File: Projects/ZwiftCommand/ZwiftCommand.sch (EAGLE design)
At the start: 17 parts, among them M1 DMP2165UW, U1 BAT-HLD-001-THM

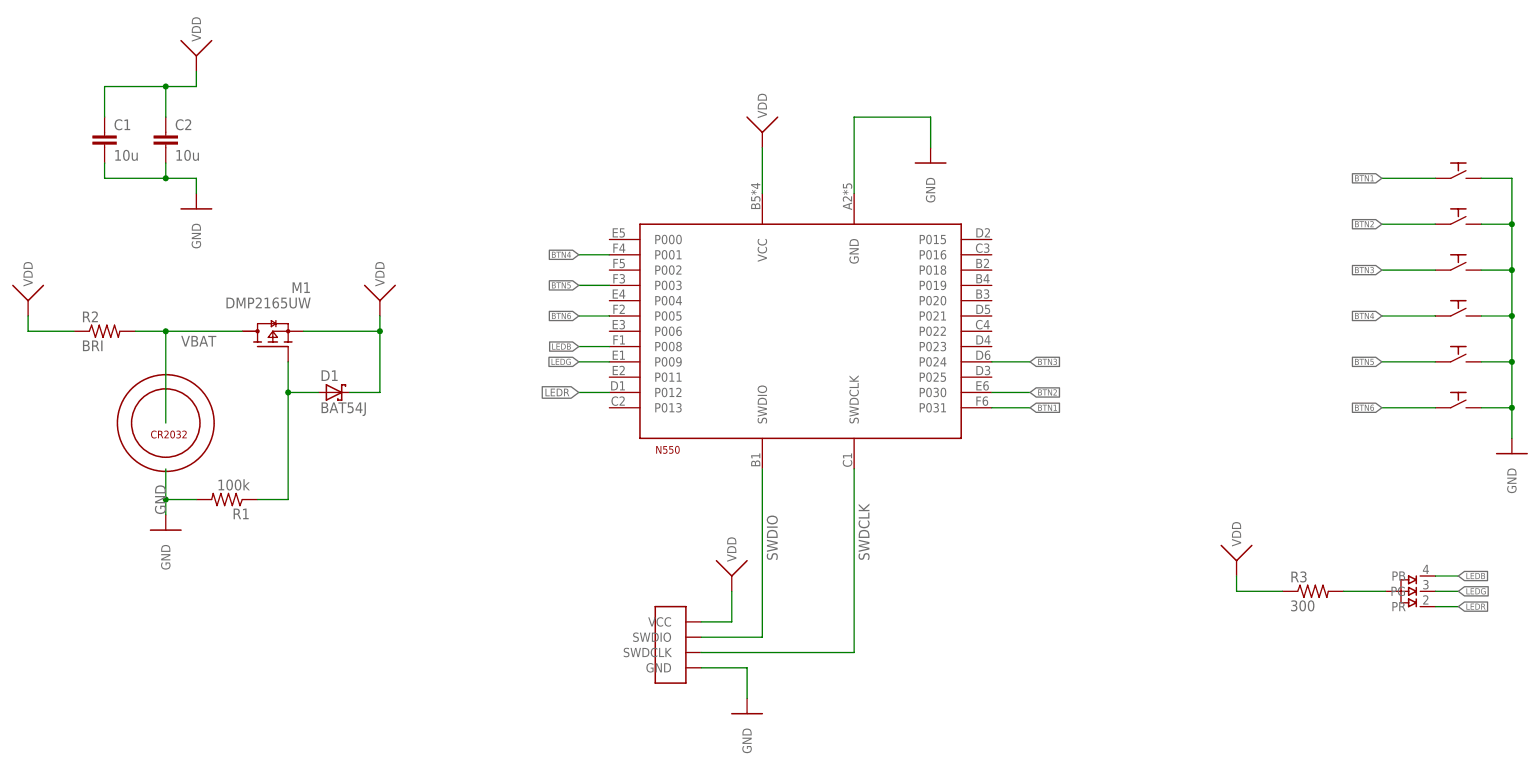
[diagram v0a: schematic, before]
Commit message: ZwiftCommand with nRF52
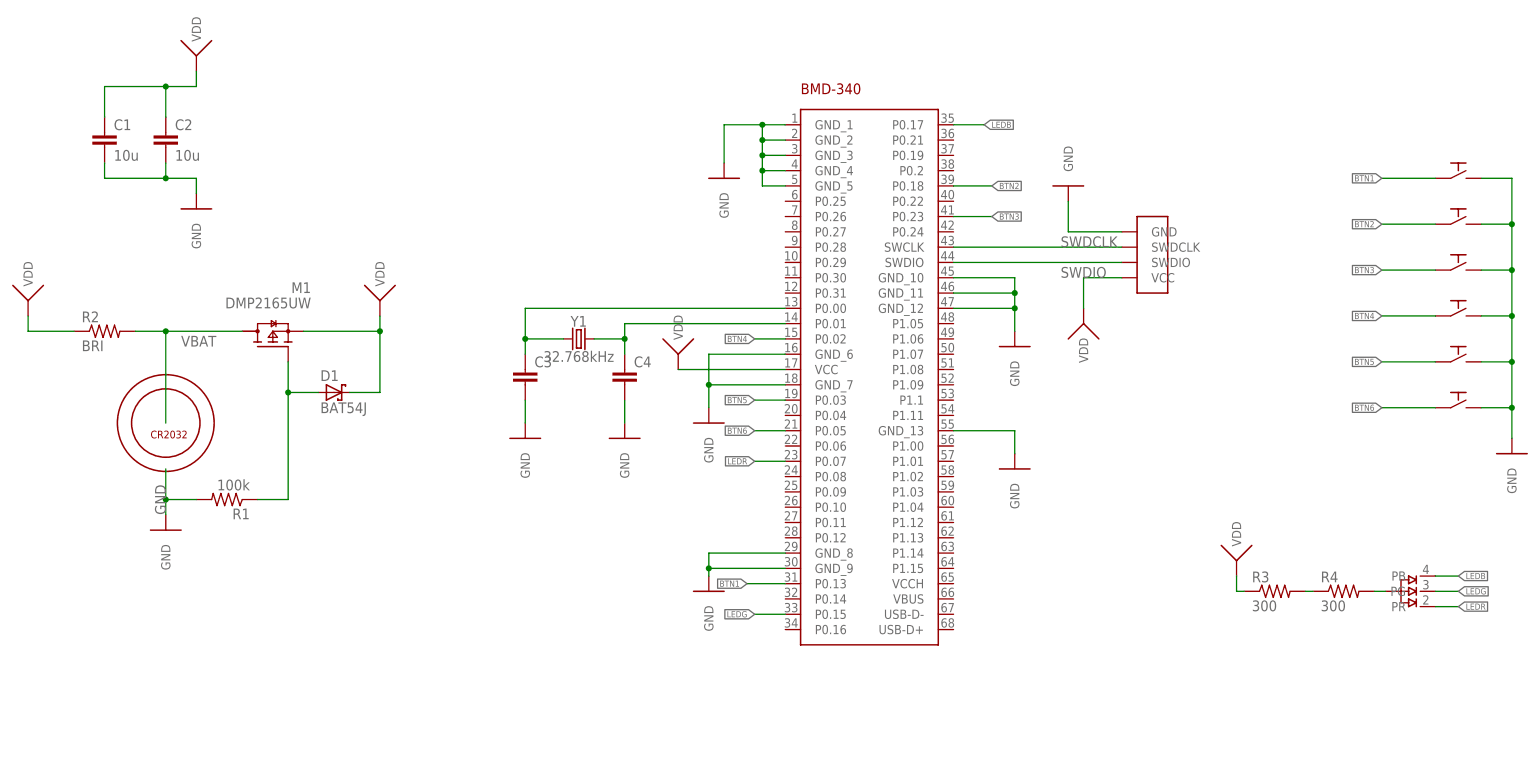
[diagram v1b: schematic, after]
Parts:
- removed U$1: N5150, N5:N5150
- added C3, C4: (no value), resistor:C-EUC0603
- added IC1: BMD-340-A-R, Rigado:BMD-340-A-R
- added R4: 300, resistor:R-US_R0603
- added Y1: 32.768kHz, SparkFun-Clocks:CRYSTAL-32.768KHZSMD-3.2X1.5
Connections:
- new net N$1: C3.1, IC1.P0.00, Y1.1
- new net N$4: C4.1, IC1.P0.01, Y1.2
- new net N$5: D2.P$1, R4.2
- net BTN1: now also IC1.P0.13; no longer U$1.P031
- net BTN2: now also IC1.P0.18; no longer U$1.P030
- net BTN3: now also IC1.P0.23; no longer U$1.P024
- net BTN4: now also IC1.P0.02; no longer U$1.P001
- net BTN5: now also IC1.P0.03; no longer U$1.P003
- net BTN6: now also IC1.P0.05; no longer U$1.P005
- net GND: now also C3.2, C4.2, IC1.GND_1, IC1.GND_10, IC1.GND_11, IC1.GND_12, IC1.GND_13, IC1.GND_2, IC1.GND_3, IC1.GND_4, IC1.GND_5, IC1.GND_6, IC1.GND_7, IC1.GND_8, IC1.GND_9; no longer U$1.GND
- net LEDB: now also IC1.P0.17; no longer U$1.P008
- net LEDG: now also IC1.P0.15; no longer U$1.P009
- net LEDR: now also IC1.P0.07; no longer U$1.P012
- net N$3: now also R4.1; no longer D2.P$1
- net SWDCLK: now also IC1.SWCLK; no longer U$1.SWDCLK
- net SWDIO: now also IC1.SWDIO; no longer U$1.SWDIO
- net VDD: now also IC1.VCC; no longer U$1.VCC
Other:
- moved on the sheet: R3
